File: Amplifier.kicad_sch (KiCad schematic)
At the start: 29 parts, among them Q1 2N3904, Q2 2N3904, Q3 2N3906, U1 NE5532

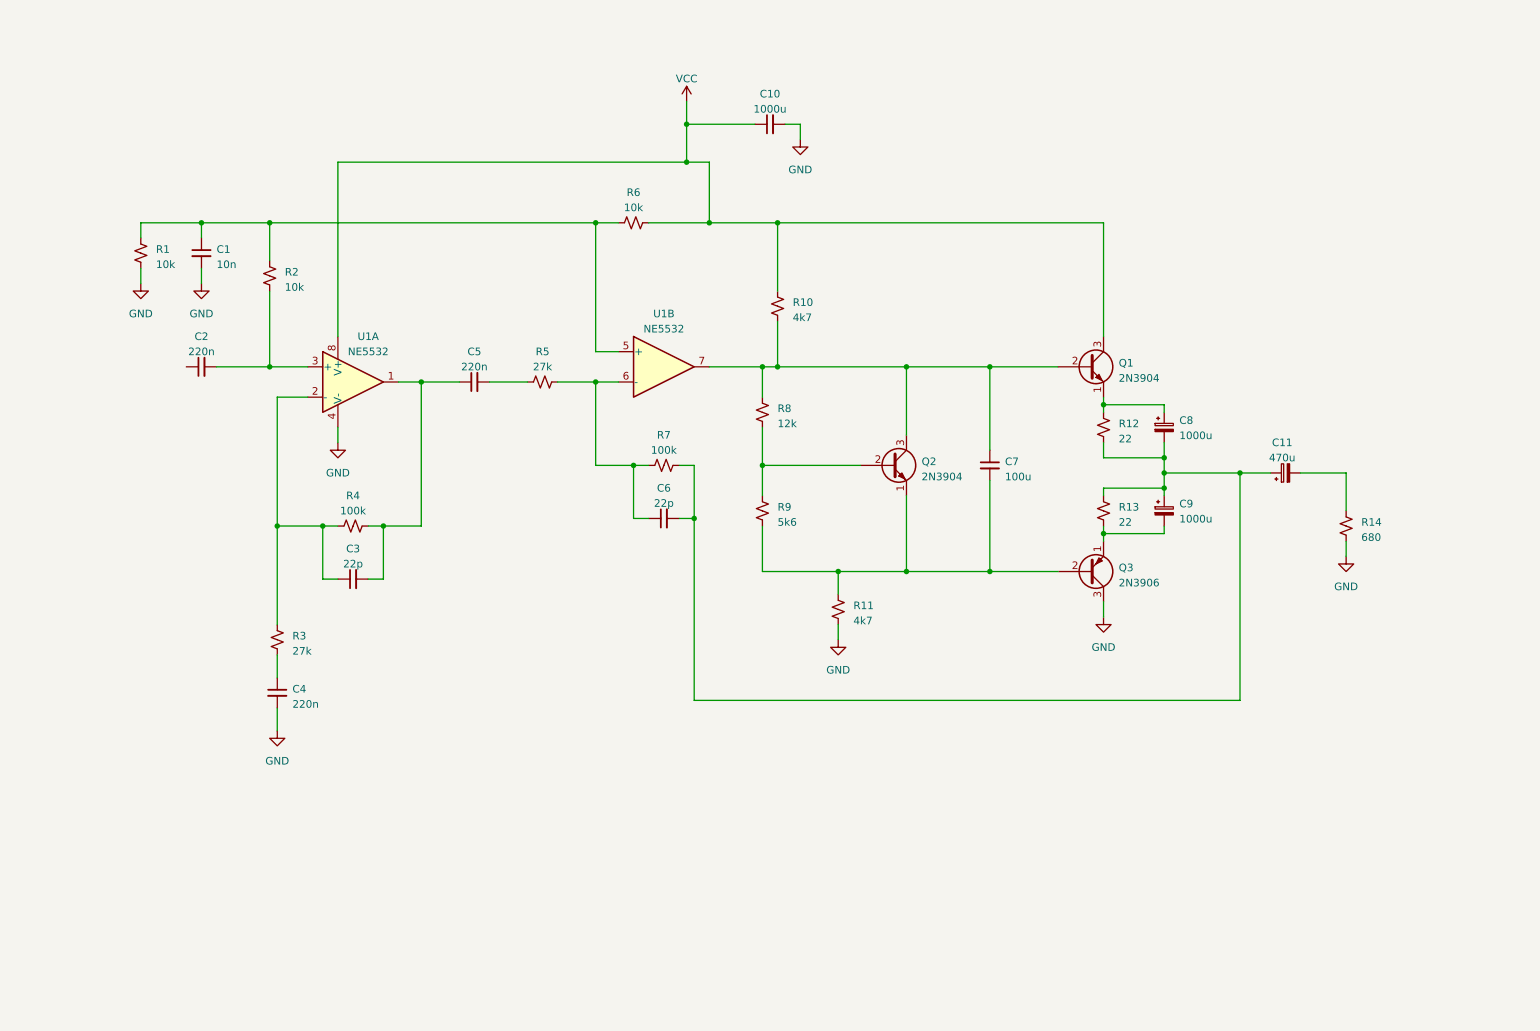
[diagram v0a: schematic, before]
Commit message: added initial footprints for components
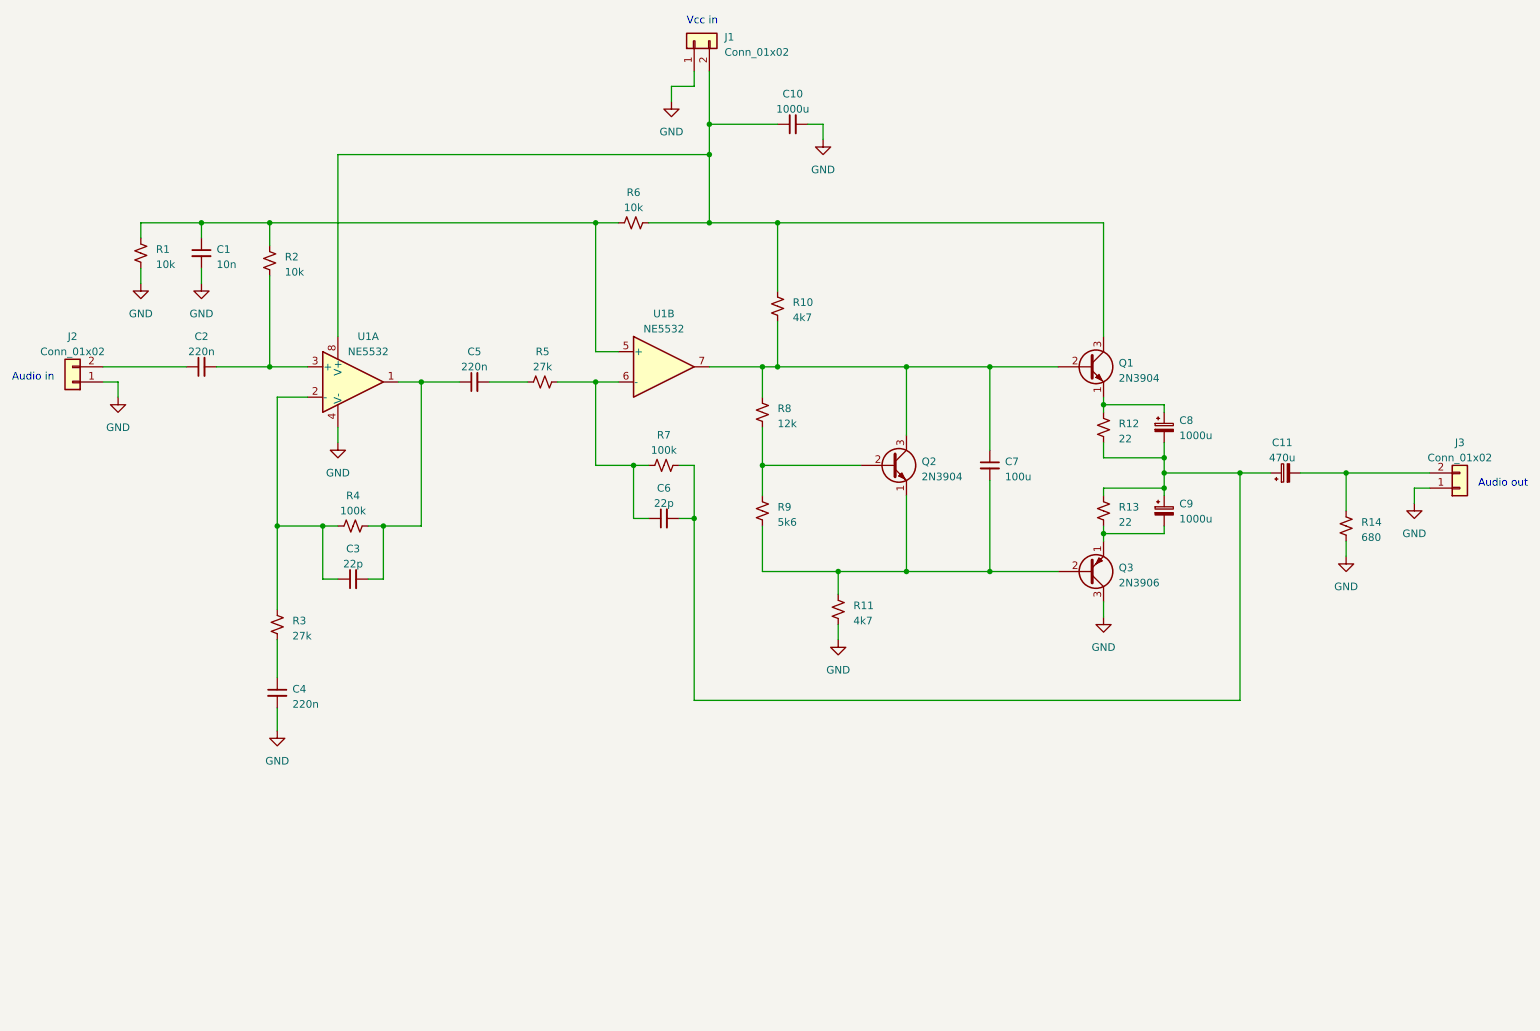
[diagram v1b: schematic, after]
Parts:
- added J1: Conn_01x02, Connector_PinHeader_2.54mm:PinHeader_1x02_P2.54mm_Vertical, symbol Connector_Generic:Conn_01x02
- added J2, J3: Conn_01x02, Connector_Wire:SolderWire-0.75sqmm_1x02_P4.8mm_D1.25mm_OD2.3mm, symbol Connector_Generic:Conn_01x02
- C1, C10, C2, C3, C4, C5, C6, C7: footprint (none) -> Capacitor_THT:C_Rect_L7.0mm_W2.0mm_P5.00mm
- C11, C8, C9: footprint (none) -> Capacitor_THT:CP_Radial_D6.3mm_P2.50mm
- R1, R10, R11, R12, R13, R14, R2, R3, R4, R5, R6, R7, R8, R9: footprint (none) -> Resistor_THT:R_Axial_DIN0204_L3.6mm_D1.6mm_P7.62mm_Horizontal
- U1: footprint (none) -> Package_DIP:DIP-8_W10.16mm
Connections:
- net GND: now also J1.1 (Pin_1), J2.1 (Pin_1), J3.1 (Pin_1)
- net at C11.2, R14.1: now also J3.2 (Pin_2)
- net at C2.1: now also J2.2 (Pin_2)
- net VCC: no longer names the net of C10.1, Q1.3 (C), R10.1, R6.2, U1.8 (V+)
- net VCC: now also J1.2 (Pin_2)
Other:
- note added: "Audio in"
- note added: "Audio out"
- note added: "Vcc in"
- moved on the sheet: C10, R2, R3

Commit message: assigned real footprints based on what we have in the EPL
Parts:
- removed C10: 1000u, Capacitor_THT:C_Rect_L7.0mm_W2.0mm_P5.00mm, symbol Device:C_Small
- added C10: 1000u, Capacitor_THT:CP_Radial_D10.0mm_P5.00mm, symbol Device:C_Polarized_Small_US
- C1: footprint Capacitor_THT:C_Rect_L7.0mm_W2.0mm_P5.00mm -> Resistor_THT:R_Axial_DIN0207_L6.3mm_D2.5mm_P10.16mm_Horizontal
- C11, C8, C9: footprint Capacitor_THT:CP_Radial_D6.3mm_P2.50mm -> Capacitor_THT:CP_Radial_D10.0mm_P5.00mm; symbol Device:C_Polarized_Small -> Device:C_Polarized_Small_US
- C7: footprint Capacitor_THT:C_Rect_L7.0mm_W2.0mm_P5.00mm -> Capacitor_THT:CP_Radial_D8.0mm_P3.50mm; symbol Device:C_Small -> Device:C_Polarized_Small_US
- J1: footprint Connector_PinHeader_2.54mm:PinHeader_1x02_P2.54mm_Vertical -> TerminalBlock:TerminalBlock_Altech_AK300-2_P5.00mm
- J2, J3: footprint Connector_Wire:SolderWire-0.75sqmm_1x02_P4.8mm_D1.25mm_OD2.3mm -> TerminalBlock:TerminalBlock_Altech_AK300-2_P5.00mm
- Q1, Q2, Q3: footprint Package_TO_SOT_THT:TO-92_Inline -> Package_TO_SOT_THT:TO-92_Inline_Wide
- R1, R10, R11, R12, R13, R14, R2, R3, R4, R5, R6, R7, R8, R9: footprint Resistor_THT:R_Axial_DIN0204_L3.6mm_D1.6mm_P7.62mm_Horizontal -> Resistor_THT:R_Axial_DIN0207_L6.3mm_D2.5mm_P10.16mm_Horizontal
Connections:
- net GND: now also C10.2
- net at J1.2 (Pin_2), Q1.3 (C), R10.1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: now also C10.1

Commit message: mid layout check-in
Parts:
- C1: footprint Resistor_THT:R_Axial_DIN0207_L6.3mm_D2.5mm_P10.16mm_Horizontal -> Capacitor_THT:C_Rect_L7.0mm_W2.5mm_P5.00mm
- C2, C3, C4, C5, C6: footprint Capacitor_THT:C_Rect_L7.0mm_W2.0mm_P5.00mm -> Capacitor_THT:C_Rect_L7.0mm_W2.5mm_P5.00mm
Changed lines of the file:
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@@
       (effects (font (size 1.27 1.27)))
     )
-    (property "Footprint" "Capacitor_THT:C_Rect_L7.0mm_W2.0mm_P5.00mm" (at 78.74 113.03 0)
+    (property "Footprint" "Capacitor_THT:C_Rect_L7.0mm_W2.5mm_P5.00mm" (at 78.74 113.03 0)
       (effects (font (size 1.27 1.27)) hide)
     )
@@
       (effects (font (size 1.27 1.27)))
     )
-    (property "Footprint" "Capacitor_THT:C_Rect_L7.0mm_W2.0mm_P5.00mm" (at 130.81 102.87 0)
+    (property "Footprint" "Capacitor_THT:C_Rect_L7.0mm_W2.5mm_P5.00mm" (at 130.81 102.87 0)
       (effects (font (size 1.27 1.27)) hide)
     )
@@
       (effects (font (size 1.27 1.27)) (justify left))
     )
-    (property "Footprint" "Resistor_THT:R_Axial_DIN0207_L6.3mm_D2.5mm_P10.16mm_Horizontal" (at 53.34 58.42 0)
+    (property "Footprint" "Capacitor_THT:C_Rect_L7.0mm_W2.5mm_P5.00mm" (at 53.34 58.42 0)
       (effects (font (size 1.27 1.27)) hide)
     )
@@
       (effects (font (size 1.27 1.27)))
     )
-    (property "Footprint" "Capacitor_THT:C_Rect_L7.0mm_W2.0mm_P5.00mm" (at 53.34 77.47 0)
+    (property "Footprint" "Capacitor_THT:C_Rect_L7.0mm_W2.5mm_P5.00mm" (at 53.34 77.47 0)
       (effects (font (size 1.27 1.27)) hide)
     )
@@
       (effects (font (size 1.27 1.27)) (justify left))
     )
-    (property "Footprint" "Capacitor_THT:C_Rect_L7.0mm_W2.0mm_P5.00mm" (at 66.04 132.08 0)
+    (property "Footprint" "Capacitor_THT:C_Rect_L7.0mm_W2.5mm_P5.00mm" (at 66.04 132.08 0)
       (effects (font (size 1.27 1.27)) hide)
     )
@@
       (effects (font (size 1.27 1.27)))
     )
-    (property "Footprint" "Capacitor_THT:C_Rect_L7.0mm_W2.0mm_P5.00mm" (at 99.06 80.01 0)
-      (effects (font (size 1.27 1.27)) hide)
-    )
+    (property "Footprint" "Capacitor_THT:C_Rect_L7.0mm_W2.5mm_P5.00mm" (at 99.06 80.01 0)
+      (effects (font (size 1.27 1.27)) hide)
+    )

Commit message: layout work and added M3 mounting holes
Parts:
- added H1, H2, H3, H4: MountingHole_Pad, MountingHole:MountingHole_3.2mm_M3_Pad_TopBottom, symbol Mechanical:MountingHole_Pad
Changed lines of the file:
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@@
+    )
+  )
+  (symbol (lib_id "Mechanical:MountingHole_Pad") (at 127 176.53 0) (unit 1)
+    (in_bom yes) (on_board yes) (dnp no) (fields_autoplaced)
+    (property "Reference" "H3" (at 129.54 174.625 0)
+      (effects (font (size 1.27 1.27)) (justify left))
+    )
+    (property "Value" "MountingHole_Pad" (at 129.54 177.165 0)
+      (effects (font (size 1.27 1.27)) (justify left))
+    )
+    (property "Footprint" "MountingHole:MountingHole_3.2mm_M3_Pad_TopBottom" (at 127 176.53 0)
+      (effects (font (size 1.27 1.27)) hide)
+    )
+    (property "Datasheet" "~" (at 127 176.53 0)
+      (effects (font (size 1.27 1.27)) hide)
+    )
+    (pin "1")
+    (instances
+      (project "Amplifier"
+        (path "/e11b4d54-e04c-40d7-a3c1-b5c4e62300dc"
+          (reference "H3") (unit 1)
+        )
+      )
     )
   )
@@
     )
   )
+  (symbol (lib_id "Mechanical:MountingHole_Pad") (at 127 161.29 0) (unit 1)
+    (in_bom yes) (on_board yes) (dnp no) (fields_autoplaced)
+    (property "Reference" "H1" (at 129.54 159.385 0)
+      (effects (font (size 1.27 1.27)) (justify left))
+    )
+    (property "Value" "MountingHole_Pad" (at 129.54 161.925 0)
+      (effects (font (size 1.27 1.27)) (justify left))
+    )
+    (property "Footprint" "MountingHole:MountingHole_3.2mm_M3_Pad_TopBottom" (at 127 161.29 0)
+      (effects (font (size 1.27 1.27)) hide)
+    )
+    (property "Datasheet" "~" (at 127 161.29 0)
+      (effects (font (size 1.27 1.27)) hide)
+    )
+    (pin "1")
+    (instances
+      (project "Amplifier"
+        (path "/e11b4d54-e04c-40d7-a3c1-b5c4e62300dc"
+          (reference "H1") (unit 1)
+        )
+      )
+    )
+  )
   (symbol (lib_id "Device:C_Small") (at 78.74 113.03 90) (unit 1)
     (in_bom yes) (on_board yes) (dnp no) (fields_autoplaced)
@@
     )
   )
+  (symbol (lib_id "Mechanical:MountingHole_Pad") (at 127 184.15 0) (unit 1)
+    (in_bom yes) (on_board yes) (dnp no) (fields_autoplaced)
+    (property "Reference" "H4" (at 129.54 182.245 0)
+      (effects (font (size 1.27 1.27)) (justify left))
+    )
+    (property "Value" "MountingHole_Pad" (at 129.54 184.785 0)
+      (effects (font (size 1.27 1.27)) (justify left))
+    )
+    (property "Footprint" "MountingHole:MountingHole_3.2mm_M3_Pad_TopBottom" (at 127 184.15 0)
+      (effects (font (size 1.27 1.27)) hide)
+    )
+    (property "Datasheet" "~" (at 127 184.15 0)
+      (effects (font (size 1.27 1.27)) hide)
+    )
+    (pin "1")
+    (instances
+      (project "Amplifier"
+        (path "/e11b4d54-e04c-40d7-a3c1-b5c4e62300dc"
+          (reference "H4") (unit 1)
+        )
+      )
+    )
+  )
   (symbol (lib_id "Device:R_Small_US") (at 110.49 80.01 90) (unit 1)
     (in_bom yes) (on_board yes) (dnp no) (fields_autoplaced)
@@
         )
       )
+    )
+  )
+  (symbol (lib_id "Mechanical:MountingHole_Pad") (at 127 168.91 0) (unit 1)
+    (in_bom yes) (on_board yes) (dnp no) (fields_autoplaced)
+    (property "Reference" "H2" (at 129.54 167.005 0)
+      (effects (font (size 1.27 1.27)) (justify left))
+    )
+    (property "Value" "MountingHole_Pad" (at 129.54 169.545 0)
+      (effects (font (size 1.27 1.27)) (justify left))
+    )
+    (property "Footprint" "MountingHole:MountingHole_3.2mm_M3_Pad_TopBottom" (at 127 168.91 0)
+      (effects (font (size 1.27 1.27)) hide)
+    )
+    (property "Datasheet" "~" (at 127 168.91 0)
+      (effects (font (size 1.27 1.27)) hide)
+    )
+    (pin "1")
+    (instances
+      (project "Amplifier"
+        (path "/e11b4d54-e04c-40d7-a3c1-b5c4e62300dc"
+          (reference "H2") (unit 1)
+        )
+      )
